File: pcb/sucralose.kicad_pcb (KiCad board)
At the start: 2 copper layers, 141.8 x 89.9 mm, 70 parts, among them M1 MountingHole_1.2mm_M1

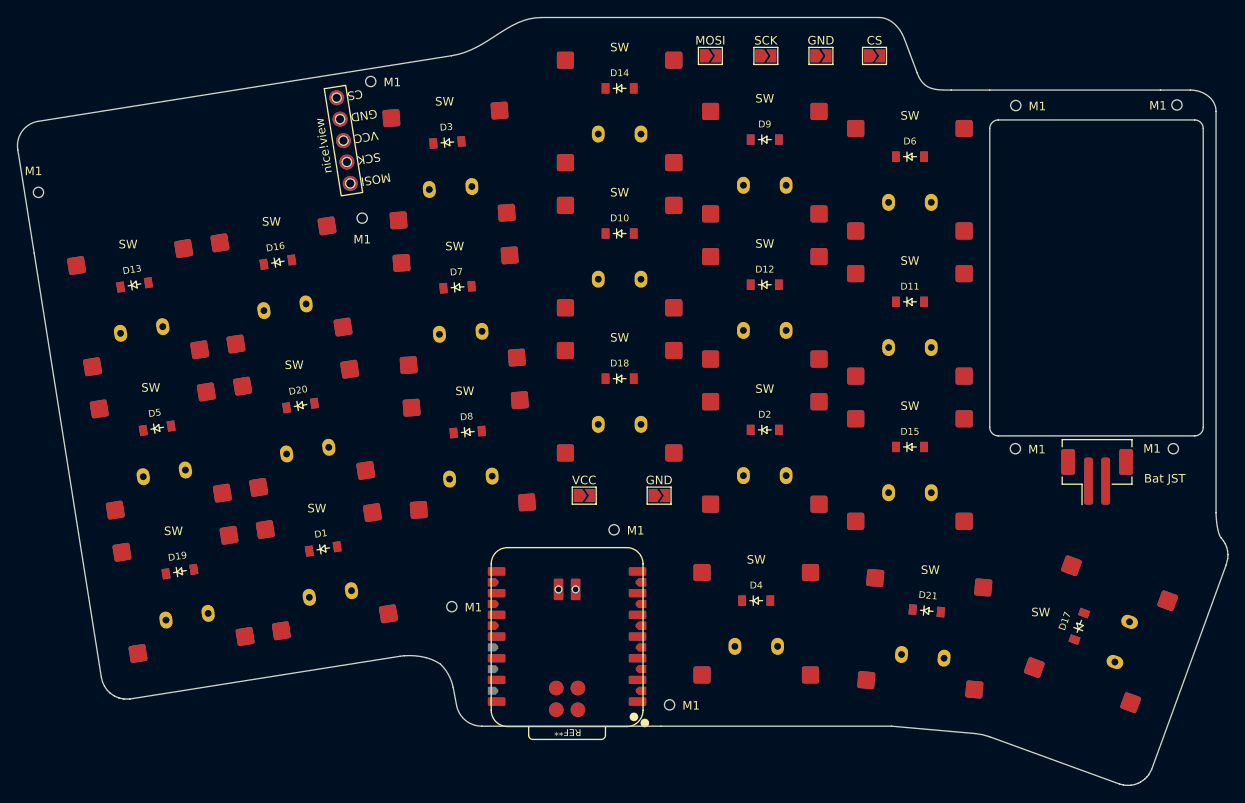
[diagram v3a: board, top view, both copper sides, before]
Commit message: Moved M1 screw holes to assist routing.
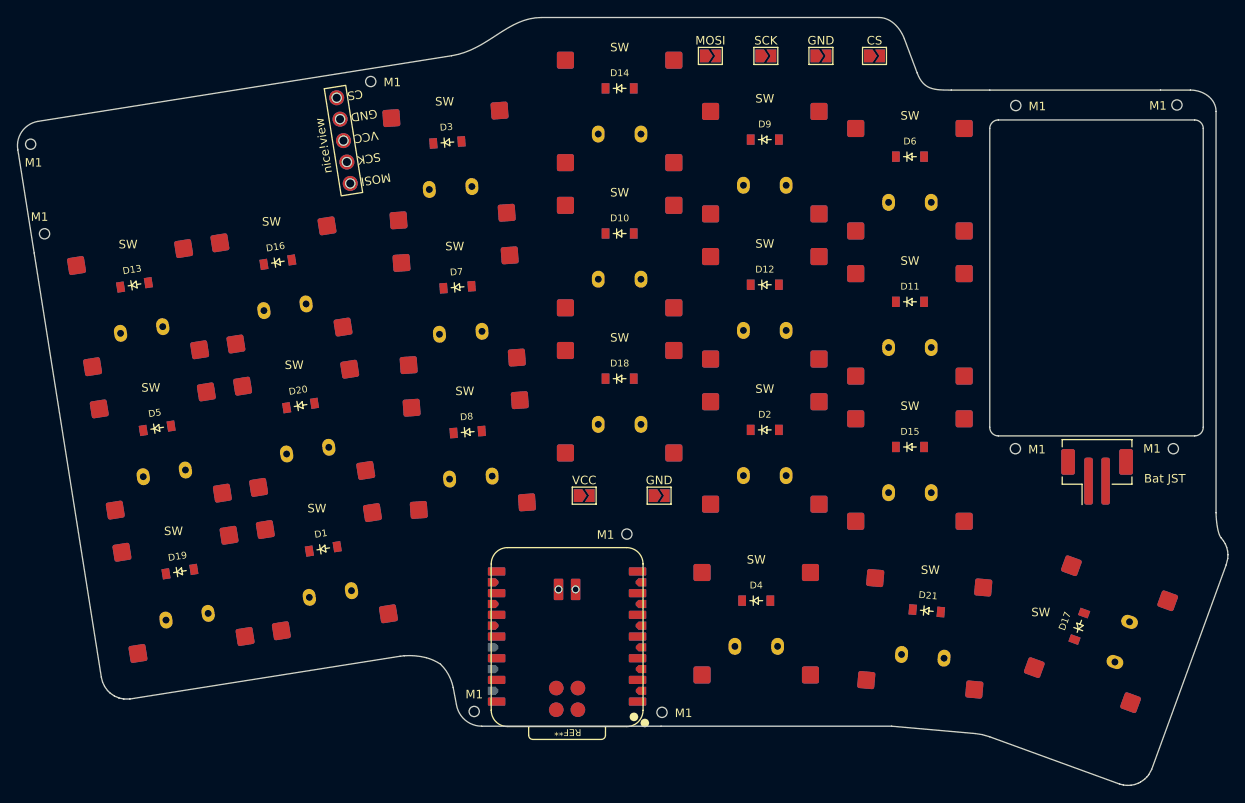
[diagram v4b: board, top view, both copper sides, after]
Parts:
- moved M1 39.8 mm to (64.7, 63.8)
- moved M1 12.6 mm to (116.6, 130.3)
- moved M1 4.90 mm to (66.3, 74.3)
- moved M1 1.58 mm to (134.5, 109.5)
- moved M1 1.25 mm to (138.6, 130.4)
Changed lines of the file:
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@@
 	(footprint "CustomParts:MountingHole_1.2mm_M1"
 		(layer "F.Cu")
-		(at 139.5 129.5)
+		(at 138.612806 130.378892)
 		(descr "Mounting Hole 1.2mm, M1, no annular, copied from M2 Mounting Hole")
 		(tags "mountinghole M2")
@@
 		(embedded_fonts no)
 	)
-	(footprint "CustomParts:MountingHole_1.2mm_M1"
-		(layer "F.Cu")
-		(at 103.5 72.5)
-		(descr "Mounting Hole 1.2mm, M1, no annular, copied from M2 Mounting Hole")
-		(tags "mountinghole M2")
-		(property "Reference" "M1"
-			(at 0 2.5 0)
-			(layer "F.SilkS")
-			(effects
-				(font
-					(size 1 1)
-					(thickness 0.15)
-				)
-			)
-		)
-		(property "Value" "MountingHole_1.2mm_M1"
-			(at 0 3.15 0)
-			(layer "F.Fab")
-			(hide yes)
-			(effects
-				(font
-					(size 1 1)
-					(thickness 0.15)
-				)
-			)
-		)
-		(property "Datasheet" ""
-			(at 0 0 0)
-			(layer "F.Fab")
-			(hide yes)
-			(effects
-				(font
-					(size 1.27 1.27)
-				)
-			)
-		)
-		(property "Description" ""
-			(at 0 0 0)
-			(layer "F.Fab")
-			(hide yes)
-			(effects
-				(font
-					(size 1.27 1.27)
-				)
-			)
-		)
-		(property "KiLib_Generator" "mounting_hardware/mounting_hole"
-			(at 0 0 0)
-			(layer "F.SilkS")
-			(hide yes)
-			(effects
-				(font
-					(size 1 1)
-					(thickness 0.15)
-				)
-			)
-		)
-		(attr exclude_from_pos_files exclude_from_bom)
-		(duplicate_pad_numbers_are_jumpers no)
-		(fp_circle
-			(center 0 0)
-			(end 1.2 0)
-			(stroke
-				(width 0.15)
-				(type solid)
-			)
-			(fill no)
-			(layer "Cmts.User")
-		)
-		(fp_circle
-			(center 0 0)
-			(end 1.3 0)
-			(stroke
-				(width 0.05)
-				(type solid)
-			)
-			(fill no)
-			(layer "F.CrtYd")
-		)
-		(fp_text user "${REFERENCE}"
-			(at 0 0 0)
-			(layer "F.Fab")
-			(effects
-				(font
-					(size 1 1)
-					(thickness 0.15)
-				)
-			)
-		)
-		(pad "" np_thru_hole circle
-			(at 0 0)
-			(size 1.2 1.2)
-			(drill 1.2)
-			(layers "*.Cu" "*.Mask")
-		)
-		(embedded_fonts no)
-	)
 	(footprint "diode_sod123_reversible"
 		(layer "F.Cu")
@@
 	(footprint "CustomParts:MountingHole_1.2mm_M1"
 		(layer "F.Cu")
-		(at 65.58624 69.479676)
+		(at 66.299106 74.3289)
 		(descr "Mounting Hole 1.2mm, M1, no annular, copied from M2 Mounting Hole")
 		(tags "mountinghole M2")
 		(property "Reference" "M1"
-			(at -0.58624 -2.479676 0)
+			(at -0.58624 -1.979676 0)
 			(layer "F.SilkS")
 			(effects
@@
 	(footprint "CustomParts:MountingHole_1.2mm_M1"
 		(layer "F.Cu")
-		(at 133 109)
+		(at 134.5 109.5)
 		(descr "Mounting Hole 1.2mm, M1, no annular, copied from M2 Mounting Hole")
 		(tags "mountinghole M2")
 		(property "Reference" "M1"
-			(at 2.523779 0.090644 0)
+			(at -2.5 0.090644 0)
 			(layer "F.SilkS")
 			(effects
@@
 	(footprint "CustomParts:MountingHole_1.2mm_M1"
 		(layer "F.Cu")
-		(at 114 118)
+		(at 116.616507 130.277058)
 		(descr "Mounting Hole 1.2mm, M1, no annular, copied from M2 Mounting Hole")
 		(tags "mountinghole M2")
 		(property "Reference" "M1"
-			(at 2.523779 0.090644 0)
+			(at 0 -2 0)
 			(layer "F.SilkS")
 			(effects
@@
 		)
 		(embedded_fonts no)
+	)
+	(footprint "CustomParts:MountingHole_1.2mm_M1"
+		(layer "F.Cu")
+		(at 64.66975 63.839924)
+		(descr "Mounting Hole 1.2mm, M1, no annular, copied from M2 Mounting Hole")
+		(tags "mountinghole M2")
+		(property "Reference" "M1"
+			(at 0.33025 2.160076 0)
+			(layer "F.SilkS")
+			(effects
+				(font
+					(size 1 1)
+					(thickness 0.15)
+				)
+			)
+		)
+		(property "Value" "MountingHole_1.2mm_M1"
+			(at 0 3.15 0)
+			(layer "F.Fab")
+			(hide yes)
+			(effects
+				(font
+					(size 1 1)
+					(thickness 0.15)
+				)
+			)
+		)
+		(property "Datasheet" ""
+			(at 0 0 0)
+			(layer "F.Fab")
+			(hide yes)
+			(effects
+				(font
+					(size 1.27 1.27)
+				)
+			)
+		)
+		(property "Description" ""
+			(at 0 0 0)
+			(layer "F.Fab")
+			(hide yes)
+			(effects
+				(font
+					(size 1.27 1.27)
+				)
+			)
+		)
+		(property "KiLib_Generator" "mounting_hardware/mounting_hole"
+			(at 0 0 0)
+			(layer "F.SilkS")
+			(hide yes)
+			(effects
+				(font
+					(size 1 1)
+					(thickness 0.15)
+				)
+			)
+		)
+		(attr exclude_from_pos_files exclude_from_bom)
+		(duplicate_pad_numbers_are_jumpers no)
+		(fp_circle
+			(center 0 0)
+			(end 1.2 0)
+			(stroke
+				(width 0.15)
+				(type solid)
+			)
+			(fill no)
+			(layer "Cmts.User")
+		)
+		(fp_circle
+			(center 0 0)
+			(end 1.3 0)
+			(stroke
+				(width 0.05)
+				(type solid)
+			)
+			(fill no)
+			(layer "F.CrtYd")
+		)
+		(fp_text user "${REFERENCE}"
+			(at 0 0 0)
+			(layer "F.Fab")
+			(effects
+				(font
+					(size 1 1)
+					(thickness 0.15)
+				)
+			)
+		)
+		(pad "" np_thru_hole circle
+			(at 0 0)
+			(size 1.2 1.2)
+			(drill 1.2)
+			(layers "*.Cu" "*.Mask")
+		)
+		(embedded_fonts no)

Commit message: Route both builds: 42 of 43 nets, copper DRC clean
622 segments, 118 vias. DRC = 88, identical to the unrouted baseline:
0 shorting_items, 0 clearance, 0 tracks_crossing, 0 hole_clearance.

Unconnected 155 -> 8: 7 are the display/battery ring pairs (front pad
and back pad of one NPTH; the soldered pin is the joint, KiCad cannot
model it) and 1 is MOSI, unrouted between the front XIAO pad 11 and
the jumper strip after 5 rip-up rounds. Every other signal reaches
both mirrored XIAO rows.

Router fixes since 1c64a1d:
  * via halo was double-counting clearance (1.0 mm to pad edge vs 0.55
    legal); that alone walled off XIAO pads 15/16. Now VIA_D/2-TRACK/2
    plus a 0.25 mm end-cap margin, vias only.
  * rip-up deleted a net's pads with its tracks (same obstacle key), so
    reroutes ran through XIAO pads (23 shorts). Static obstacles are
    snapshotted and restored.
  * tie.py is idempotent (refuses a second pass on the same result).

User changes that mattered: jumper strip 5 -> 6.5 mm pitch (c347180),
M1 holes moved (4c817b0). Round-1 failures went 5 -> 3, all at the
XIAO edge.
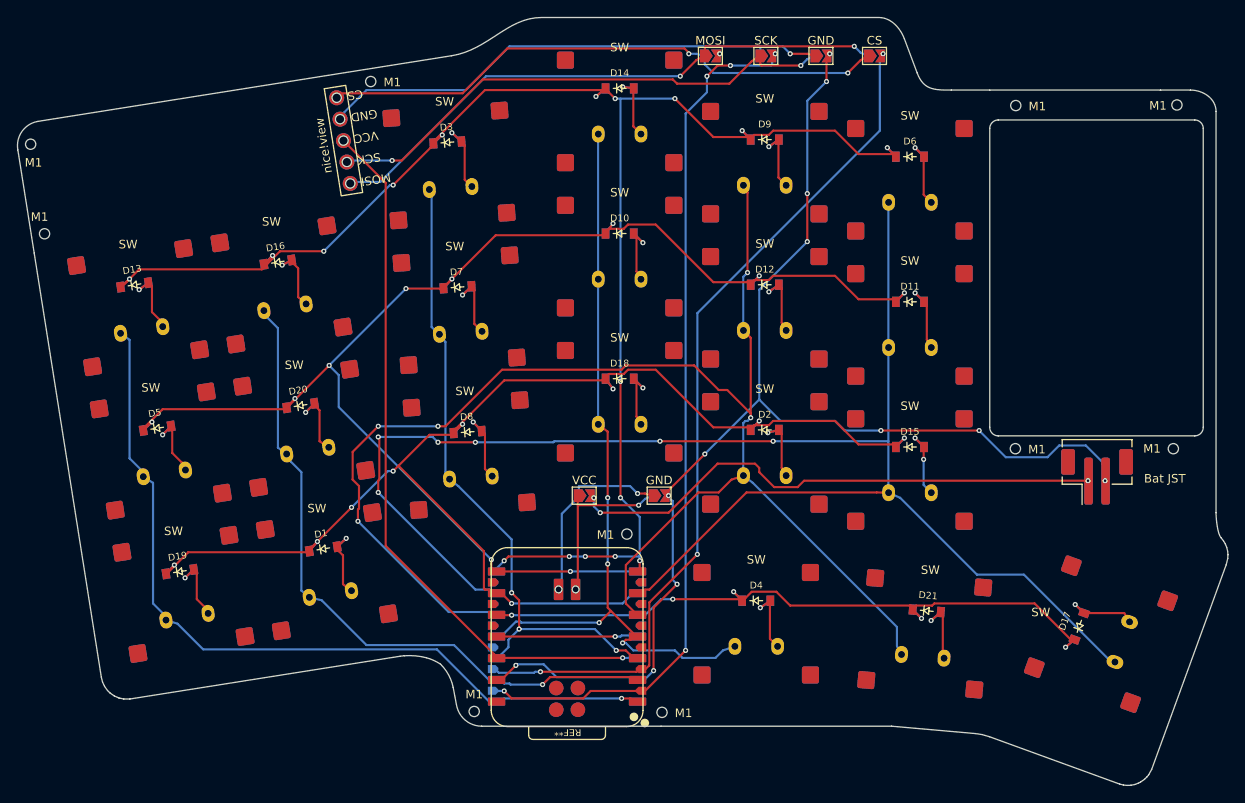
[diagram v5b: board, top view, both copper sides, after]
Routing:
- net ROW0: track 0.00 -> 196.3 mm, vias 0 -> 17
- net COL5: track 0.00 -> 188.1 mm, vias 0 -> 6
- net COL4: track 0.00 -> 170.6 mm, vias 0 -> 5
- net ROW1: track 0.00 -> 169.1 mm, vias 0 -> 10
- net ROW2: track 0.00 -> 155.1 mm, vias 0 -> 9
- net GND: track 0.00 -> 150.0 mm, vias 0 -> 12
- net SCK: track 0.00 -> 103.6 mm, vias 0 -> 5
- net CS: track 0.00 -> 102.1 mm, vias 0 -> 3
- net COL0: track 0.00 -> 95.1 mm, vias 0 -> 1
- net COL3: track 0.00 -> 91.8 mm, vias 0 -> 4
- net VCC: track 0.00 -> 83.7 mm, vias 0 -> 1
- net ROW3: track 0.00 -> 80.4 mm, vias 0 -> 5
- net COL1: track 0.00 -> 78.7 mm, vias 0 -> 1
- net COL2: track 0.00 -> 75.5 mm, vias 0 -> 3
- net DISP_H1: track 0.00 -> 67.3 mm, vias 0 -> 2
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
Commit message: Fully routed, both builds: 43/43 nets, DRC 88 (= unrouted baseline)
MOSI moved D10 -> D4 (P0.04, fast pin per nRF52840 PS); COL4 -> D10.
All three display lines now on spec-rated pins. docs/PINOUT.md carries
the new table, kscan block, and a spi3 pinctrl for the display.

640 segments, 127 vias, 0 shorts / clearance / crossing / hole hits.
Unconnected 7 = the five display and two battery ring pairs (front and
back pad of one NPTH; the soldered pin joins them).

Router: search cap was 400k expansions, set for the 0.25 grid and never
rescaled at 0.125; it was aborting long nets mid-board and reporting
them unroutable. Lifted to 3M: SCK routed first pass. Orthogonal turns
now require the outer corner cell clear (DRC caught a 0.192 mm stair).
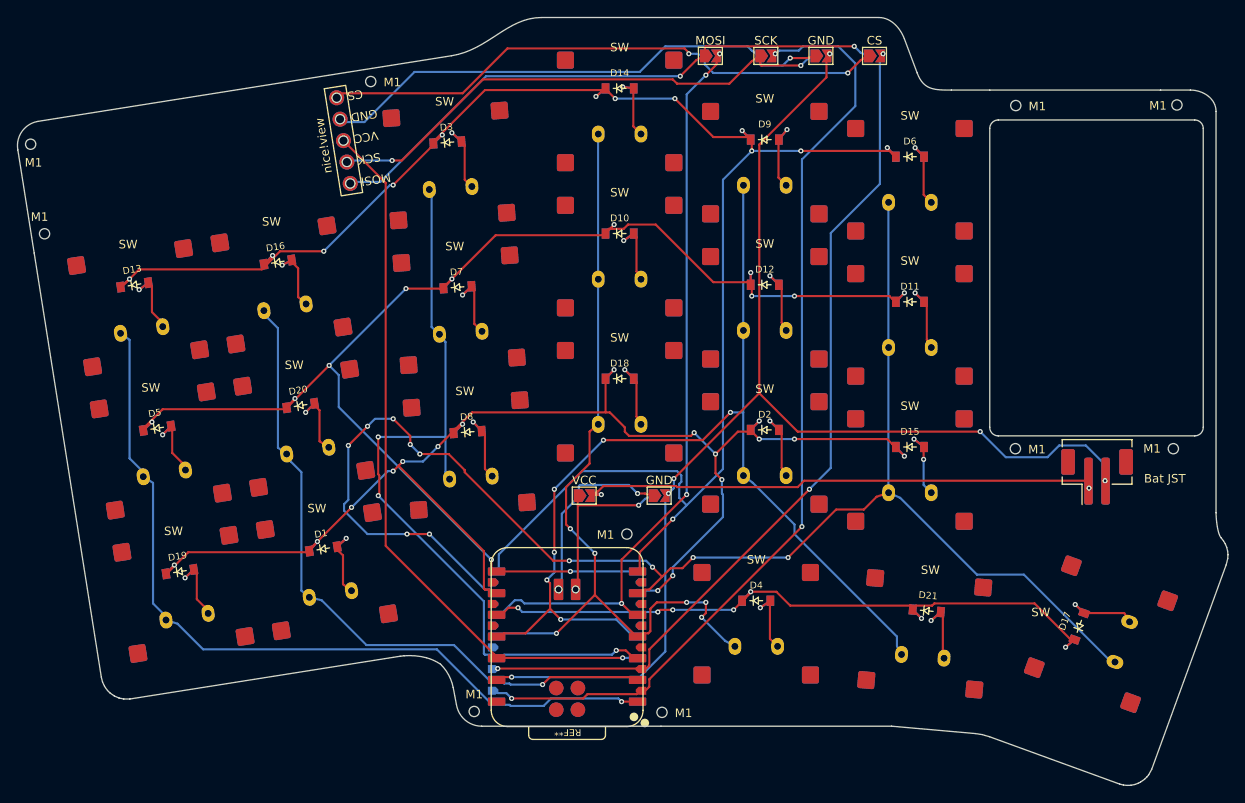
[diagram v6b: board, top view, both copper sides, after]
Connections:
- REF** pad 11: MOSI -> COL4 (x2)
- REF** pad 5: COL4 -> MOSI (x2)
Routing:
- net MOSI: track 17.5 -> 87.4 mm, vias 2 -> 4
- net COL4: track 170.6 -> 122.0 mm, vias 5 -> 6
- net COL2: track 75.5 -> 92.0 mm
- net ROW0: track 196.3 -> 208.4 mm, vias 17 -> 13
- net SCK: track 103.6 -> 114.1 mm, vias 5 -> 3
- net COL5: track 188.1 -> 178.7 mm, vias 6 -> 11
- net ROW2: track 155.1 -> 161.5 mm, vias 9 -> 17
- net COL3: track 91.8 -> 95.7 mm, vias 4 -> 6
- net GND: track 150.0 -> 147.7 mm, vias 12 -> 6
- net BAT_P: track 65.0 -> 63.3 mm, vias 3 -> 2
- net ROW3: track 80.4 -> 80.8 mm, vias 5 -> 7
- net ROW1: track 169.1 -> 168.8 mm, vias 10 -> 12

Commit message: Silk: switch labels C<col> R<row> both faces; Splenda packet logo front+back (traced, 11.5 mm, top-left)
Labels derived from netlist (switch pad -> COL, key net -> diode -> ROW), not hand-typed.
Logo: potracer + shapely, holes stitched into single-ring gr_poly; verified in the
F.SilkS/B.SilkS SVG export (back mirrored, reads correctly). Copper untouched: DRC 88,
7 unconnected = ring pairs, audit 0. scripts/silk_*.py regenerate both.
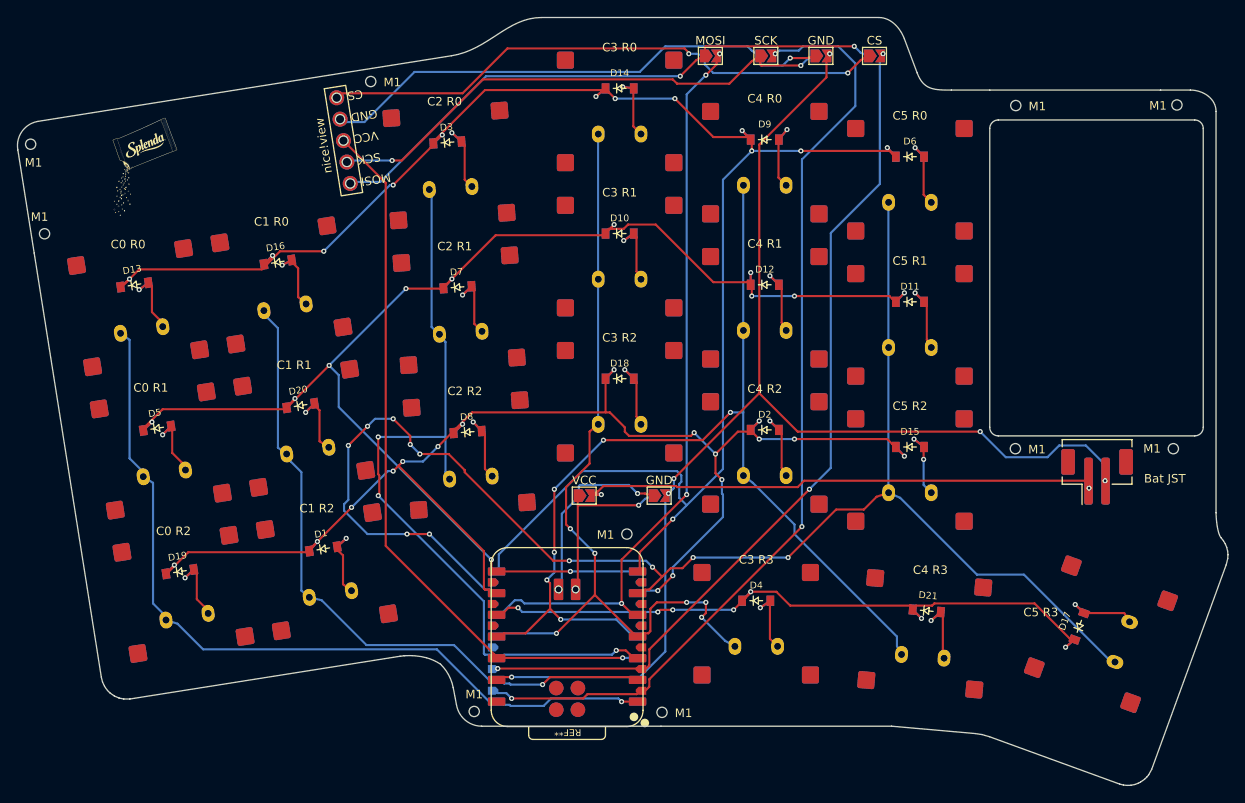
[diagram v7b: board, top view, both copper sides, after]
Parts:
- C0 R0: renamed from SW
- C0 R1: renamed from SW
- C0 R2: renamed from SW
- C1 R0: renamed from SW
- C1 R1: renamed from SW
- C1 R2: renamed from SW
- C2 R0: renamed from SW
- C2 R1: renamed from SW
- C2 R2: renamed from SW
- C3 R0: renamed from SW
- C3 R1: renamed from SW
- C3 R2: renamed from SW
- C3 R3: renamed from SW
- C4 R0: renamed from SW
- C4 R1: renamed from SW
- C4 R2: renamed from SW
- C4 R3: renamed from SW
- C5 R0: renamed from SW
- C5 R1: renamed from SW
- C5 R2: renamed from SW
- C5 R3: renamed from SW
